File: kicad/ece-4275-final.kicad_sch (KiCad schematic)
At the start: 10 parts, among them U1 ESP32-S3

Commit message: finish motor driver module
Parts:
- removed C1, C10, C3, C5, C8: 100nF, symbol Device:C
- removed C11, C12, C7, C9: 10uF, symbol Device:C
- removed U1: ESP32-S3, Package_DFN_QFN:QFN-56-1EP_7x7mm_P0.4mm_EP4x4mm, symbol MCU_Espressif:ESP32-S3
- added U2: ESP32-C6-MINI-1, RF_Module:ESP32-C6-MINI-1, symbol RF_Module:ESP32-C6-MINI-1
- added U4: (no value), PCM_Espressif:ESP32-P4, symbol PCM_Espressif:ESP32-P4
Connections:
- new net: U2.1 (GND), U2.11 (GND), U2.14 (GND), U2.2 (GND), U2.36 (GND), U2.37 (GND), U2.38 (GND), U2.39 (GND), U2.40 (GND), U2.41 (GND), U2.42 (GND), U2.43 (GND), U2.44 (GND), U2.45 (GND), U2.46 (GND), U2.47 (GND), U2.48 (GND), U2.49 (GND), U2.50 (GND), U2.51 (GND), U2.52 (GND), U2.53 (GND)
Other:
- sheet Stepper Motor Module ports: added A1, A2, B1, B2, CLK, CS, DIAG0_SWN, DIAG1_SWP, DRV_ENA, ENC_A_DCIN, ENC_B_DCEN, ENC_N_DCO, REFL_DIR, REFL_STEP, SD_MODE, SPI_MISO, SPI_MODE, SPI_MOSI, SPI_SCK, TST_MODE; removed none

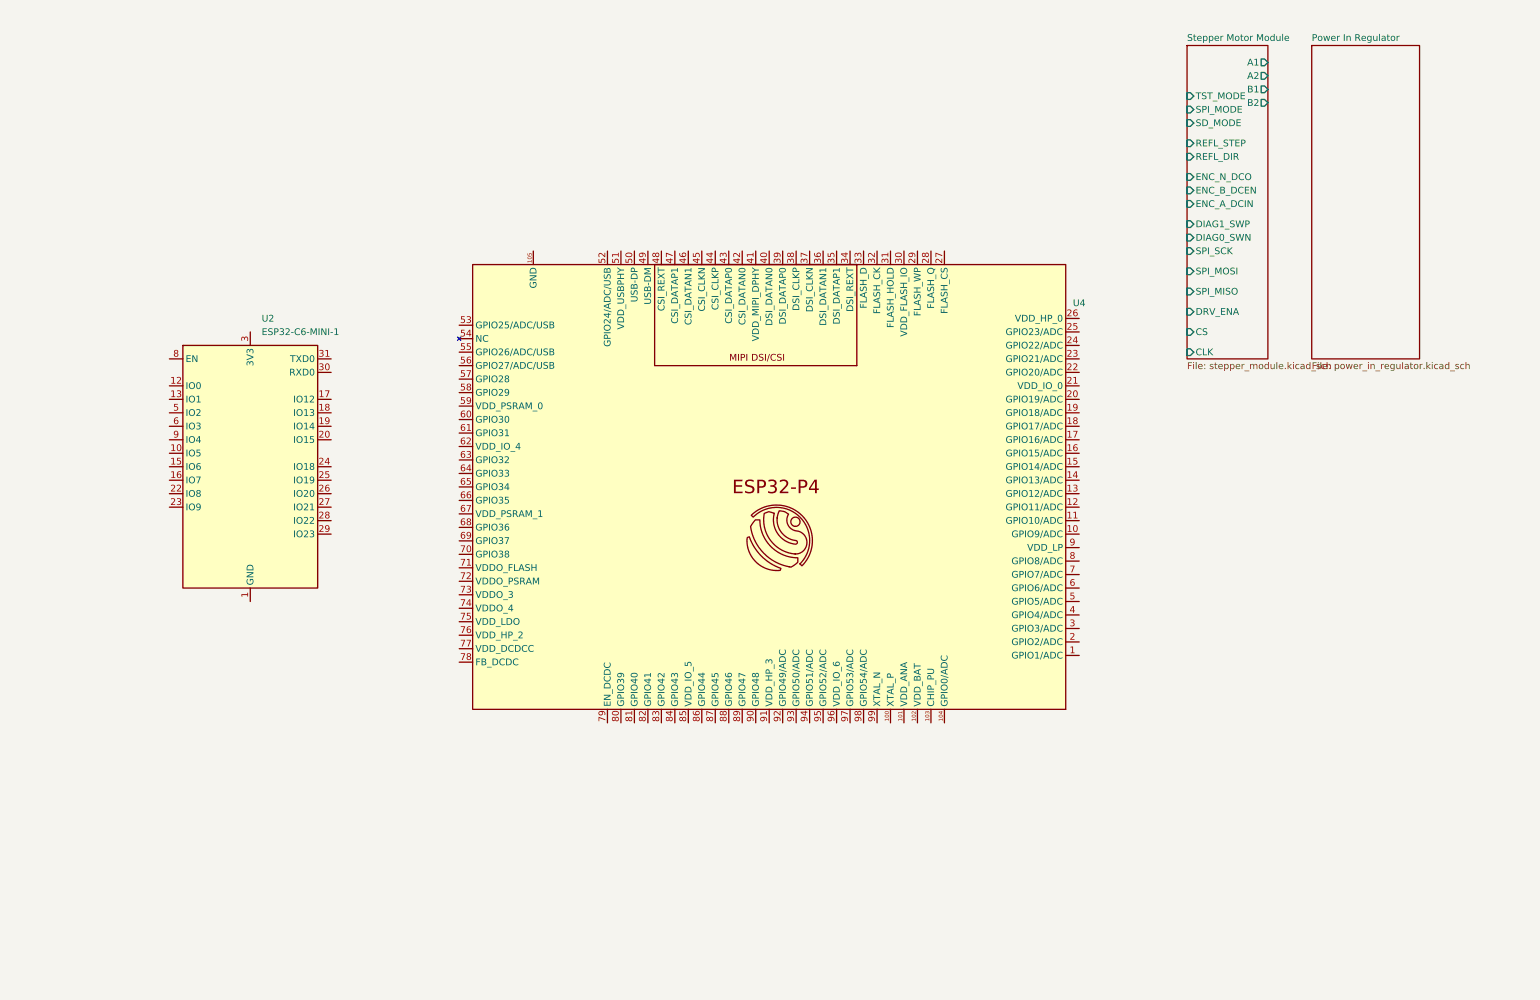
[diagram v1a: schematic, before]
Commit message: add usb connector
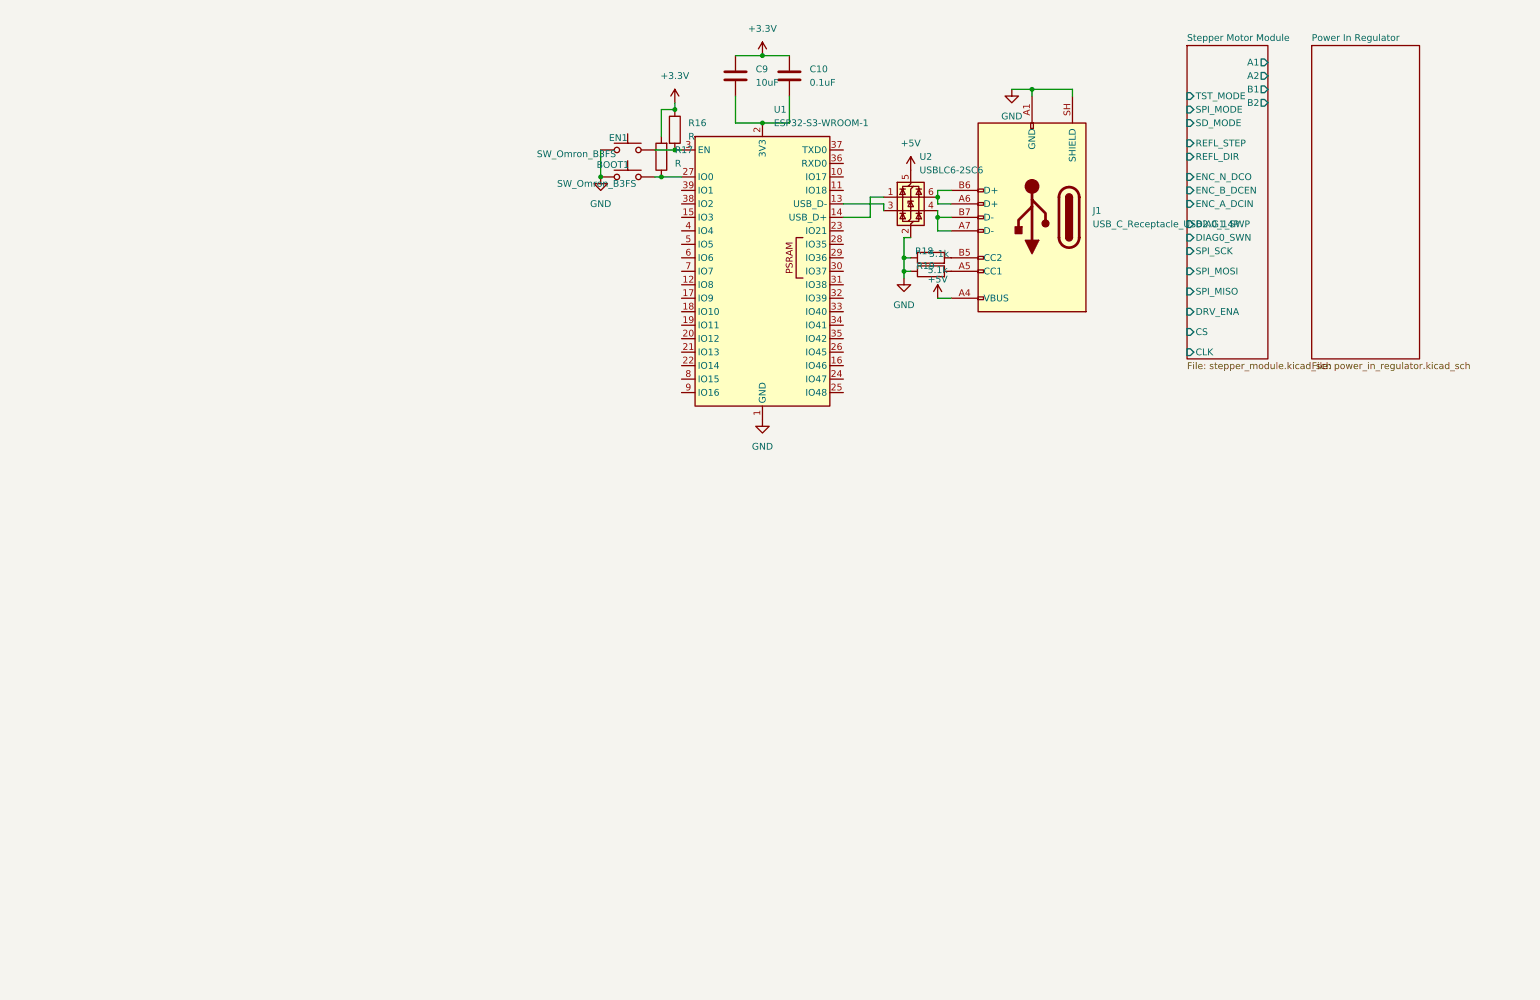
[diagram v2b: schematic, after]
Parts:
- removed U2: ESP32-C6-MINI-1, RF_Module:ESP32-C6-MINI-1, symbol RF_Module:ESP32-C6-MINI-1
- removed U4: (no value), PCM_Espressif:ESP32-P4, symbol PCM_Espressif:ESP32-P4
- added BOOT1, EN1: SW_Omron_B3FS, symbol Switch:SW_Omron_B3FS
- added C10: 0.1uF, symbol Device:C
- added C9: 10uF, symbol Device:C
- added J1: USB_C_Receptacle_USB2.0_14P, Connector_USB:USB_C_Receptacle_GCT_USB4085, symbol Connector:USB_C_Receptacle_USB2.0_14P
- added R16, R17: R, symbol Device:R
- added R18, R19: 5.1k, symbol Device:R
- added U1: ESP32-S3-WROOM-1, RF_Module:ESP32-S3-WROOM-1, symbol RF_Module:ESP32-S3-WROOM-1
- added U2: USBLC6-2SC6, Package_TO_SOT_SMD:SOT-23-6, symbol Power_Protection:USBLC6-2SC6
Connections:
- new net: U1.13 (USB_D-), U2.3 (I/O2)
- new net: U1.14 (USB_D+), U2.1 (I/O1)
- new net: C10.2, C9.2, U1.2 (3V3)
- new net: BOOT1.2, R17.1, U1.27 (IO0)
- new net: EN1.2, R16.2, U1.3 (EN)
- new net: J1.B5 (CC2), R18.2
- new net: J1.A7 (D-), J1.B7 (D-), U2.4 (I/O2)
- new net: J1.A6 (D+), J1.B6 (D+), U2.6 (I/O1)
- new net: J1.A5 (CC1), R19.2
- new net +3.3V: C10.1, C9.1, R16.1, R17.2
- new net +5V: J1.A4 (VBUS), J1.A9 (VBUS), J1.B4 (VBUS), J1.B9 (VBUS), U2.5 (VBUS)
- new net GND: BOOT1.1, EN1.1, J1.A1 (GND), J1.A12 (GND), J1.B1 (GND), J1.B12 (GND), J1.SH (SHIELD), R18.1, R19.1, U1.1 (GND), U1.40 (GND), U1.41 (GND), U2.2 (GND)

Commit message: edit a lot of stuff
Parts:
- added J3, J4: Conn_01x08, Connector_PinHeader_2.54mm:PinHeader_1x08_P2.54mm_Vertical, symbol Connector_Generic:Conn_01x08
- added J5: Conn_01x02, Connector_PinHeader_2.54mm:PinHeader_1x02_P2.54mm_Vertical, symbol Connector_Generic:Conn_01x02
- added Q9: AO3400A, Package_TO_SOT_SMD:SOT-23, symbol Transistor_FET:AO3400A
- BOOT1, EN1: footprint (none) -> Button_Switch_SMD:SW_Push_1P1T-SH_NO_CK_KMR2xxG
- C10, C9: footprint (none) -> Capacitor_SMD:C_0402_1005Metric
- R16, R17, R18, R19: footprint (none) -> Resistor_SMD:R_0402_1005Metric
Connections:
- net GND: now also J3.1 (Pin_1), J3.2 (Pin_2), J3.3 (Pin_3), J3.4 (Pin_4), J3.5 (Pin_5), J3.6 (Pin_6), J3.7 (Pin_7), J3.8 (Pin_8), Q9.2 (S)
- new net: J5.1 (Pin_1), Q9.3 (D)

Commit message: update pcb routing:
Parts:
- added J6: STEPPER_1_JST_XH, Connector_JST:JST_XH_B4B-XH-A_1x04_P2.50mm_Vertical, symbol Connector_Generic:Conn_01x04
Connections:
- net Stepper Motor Module/A1: now also J6.2 (Pin_2)
- net Stepper Motor Module/A2: now also J6.1 (Pin_1)
- net Stepper Motor Module/B1: now also J6.4 (Pin_4)
- net Stepper Motor Module/B2: now also J6.3 (Pin_3)
- net DRV_MOSI: now reaches U1.19 (IO11)
- net DRV_SCK: now reaches U1.20 (IO12)
- net DRV_MISO: now reaches U1.21 (IO13)
- net DRV_ENA: now reaches U1.22 (IO14)

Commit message: finish routing gpios
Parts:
- removed J3, J4: Conn_01x08, Connector_PinHeader_2.54mm:PinHeader_1x08_P2.54mm_Vertical, symbol Connector_Generic:Conn_01x08
- removed J5: Conn_01x02, Connector_PinHeader_2.54mm:PinHeader_1x02_P2.54mm_Vertical, symbol Connector_Generic:Conn_01x02
- removed Q9: AO3400A, Package_TO_SOT_SMD:SOT-23, symbol Transistor_FET:AO3400A
- added J1: LED_CONN_1, Connector_JST:JST_PH_B3B-PH-K_1x03_P2.00mm_Vertical, symbol Connector_Generic:Conn_01x03
- added J2: LED_CONN_0, Connector_JST:JST_PH_B3B-PH-K_1x03_P2.00mm_Vertical, symbol Connector_Generic:Conn_01x03
- added J3: TX_RX, Connector_JST:JST_PH_B2B-PH-K_1x02_P2.00mm_Vertical, symbol Connector_Generic:Conn_01x02
- added J4: GPIO_38_48, Connector_PinHeader_2.54mm:PinHeader_1x09_P2.54mm_Vertical, symbol Connector_Generic:Conn_01x09
- added R2, R21: 330, Resistor_SMD:R_0402_1005Metric, symbol Device:R
- renumbered C9 to C1, C10 to C2, J1 to J5, R17 to R1, R16 to R3, R18 to R4, R19 to R5
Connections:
- net +5V: now also J1.3 (Pin_3), J2.3 (Pin_3)
- net GND: now also J1.2 (Pin_2), J2.2 (Pin_2)
- net Two Pin Fan2/IN: now reaches U1.12 (IO8)
- net at U1.16 (IO46): now also J4.7 (Pin_7)
- net Two Pin Fan1/IN: now reaches U1.17 (IO9)
- net Two Pin Fan/IN: now reaches U1.18 (IO10)
- net at U1.24 (IO47): now also J4.8 (Pin_8)
- net at U1.25 (IO48): now also J4.9 (Pin_9)
- net at U1.26 (IO45): now also J4.6 (Pin_6)
- net at U1.31 (IO38): now also J4.1 (Pin_1)
- net at U1.32 (IO39): now also J4.2 (Pin_2)
- net at U1.33 (IO40): now also J4.3 (Pin_3)
- net at U1.34 (IO41): now also J4.4 (Pin_4)
- net at U1.35 (IO42): now also J4.5 (Pin_5)
- net at U1.36 (RXD0): now also J3.2 (Pin_2)
- net at U1.37 (TXD0): now also J3.1 (Pin_1)
- net LIMIT_1: now reaches U1.38 (IO2)
- net LIMIT_0: now reaches U1.39 (IO1)
- net LIMIT_2: now reaches U1.4 (IO4)
- net at U1.6 (IO6): now also R2.2
- net at U1.7 (IO7): now also R21.2
- new net: J1.1 (Pin_1), R21.1
- new net: J2.1 (Pin_1), R2.1
- no-connect marks 0 -> 4
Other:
- added sheet Three Limit Switches (three_limit_switch.kicad_sch)
- added sheet Two Pin Fan (two_pin_fan.kicad_sch)
- added sheet Two Pin Fan1 (two_pin_fan.kicad_sch)
- added sheet Two Pin Fan2 (two_pin_fan.kicad_sch)

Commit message: final?
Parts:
- added C19, C20: 0.1uF, Capacitor_SMD:C_0402_1005Metric, symbol Device:C
- added POWER_LED1: LED, LED_THT:LED_D10.0mm, symbol Device:LED
- added R22, R23: 10k, Resistor_SMD:R_0402_1005Metric, symbol Device:R
- added R24: 680, Resistor_SMD:R_0402_1005Metric, symbol Device:R
- added THERM1: THERM1, Connector_JST:JST_PH_B2B-PH-K_1x02_P2.00mm_Vertical, symbol Connector_Generic:Conn_01x02
- added THERM2: THERM2, Connector_JST:JST_PH_B2B-PH-K_1x02_P2.00mm_Vertical, symbol Connector_Generic:Conn_01x02
- R1, R3: value R -> 10k
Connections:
- net +3.3V: now also R22.1, R23.1, R24.2
- net DRV_1_CS: now also U1.8 (IO15)
- net DRV_1_DIR: now also U1.11 (IO18)
- net DRV_1_STEP: now also U1.9 (IO16)
- net GND: now also POWER_LED1.1 (K), THERM1.2 (Pin_2), THERM2.2 (Pin_2)
- net LIMIT_2: now also U1.10 (IO17); no longer U1.4 (IO4)
- net at U1.5 (IO5): now also C20.1
- new net: C19.1, U1.4 (IO4)
- new net: C19.2, R22.2, THERM1.1 (Pin_1)
- new net: C20.2, R23.2, THERM2.1 (Pin_1)
- new net: POWER_LED1.2 (A), R24.1
